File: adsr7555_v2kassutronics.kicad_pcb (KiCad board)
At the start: 2 copper layers, 68.6 x 104.1 mm, 47 parts, among them J1 Power, J2 GateIn, J5 Atn Out, J6 Output, Q1 3904, Q2 3904, Q3 3904, Q4 3904, SW1 SW_Push, U1 7555, U2 TL074

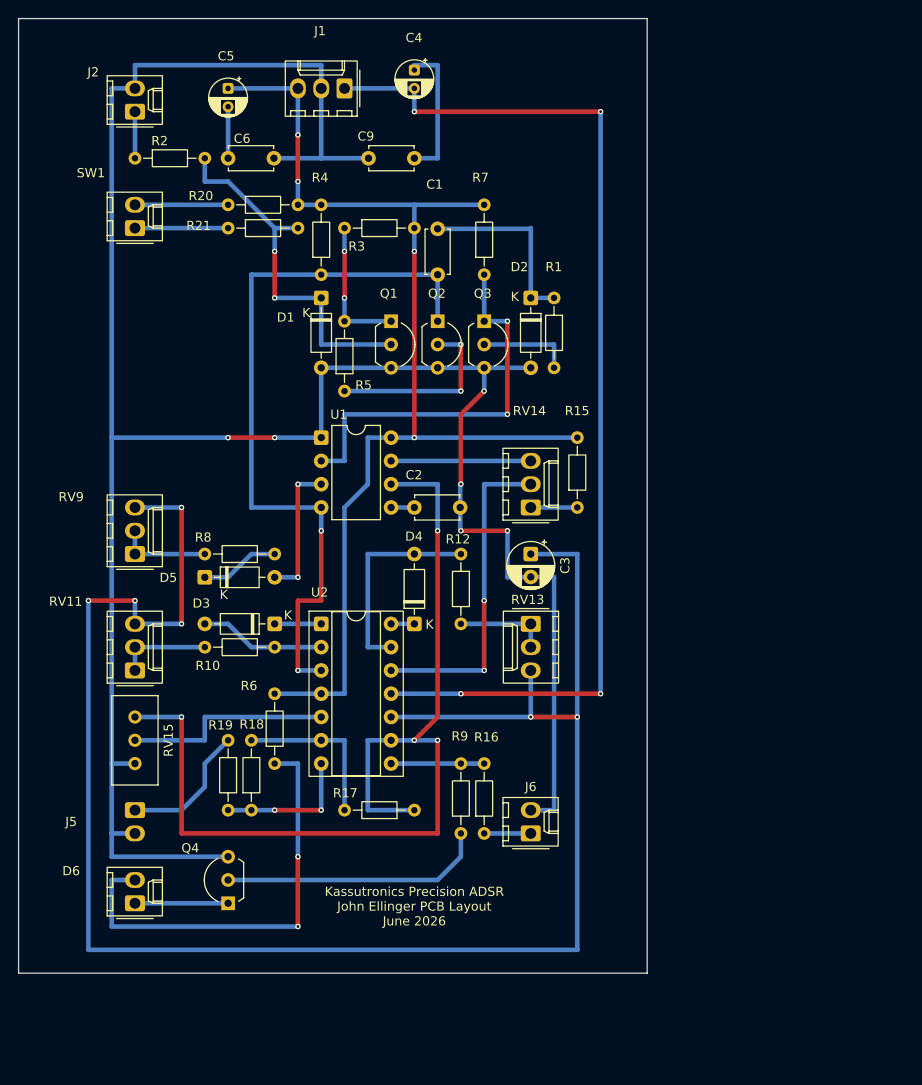
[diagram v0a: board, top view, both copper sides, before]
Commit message: archived v1 to jail. Redo for v2
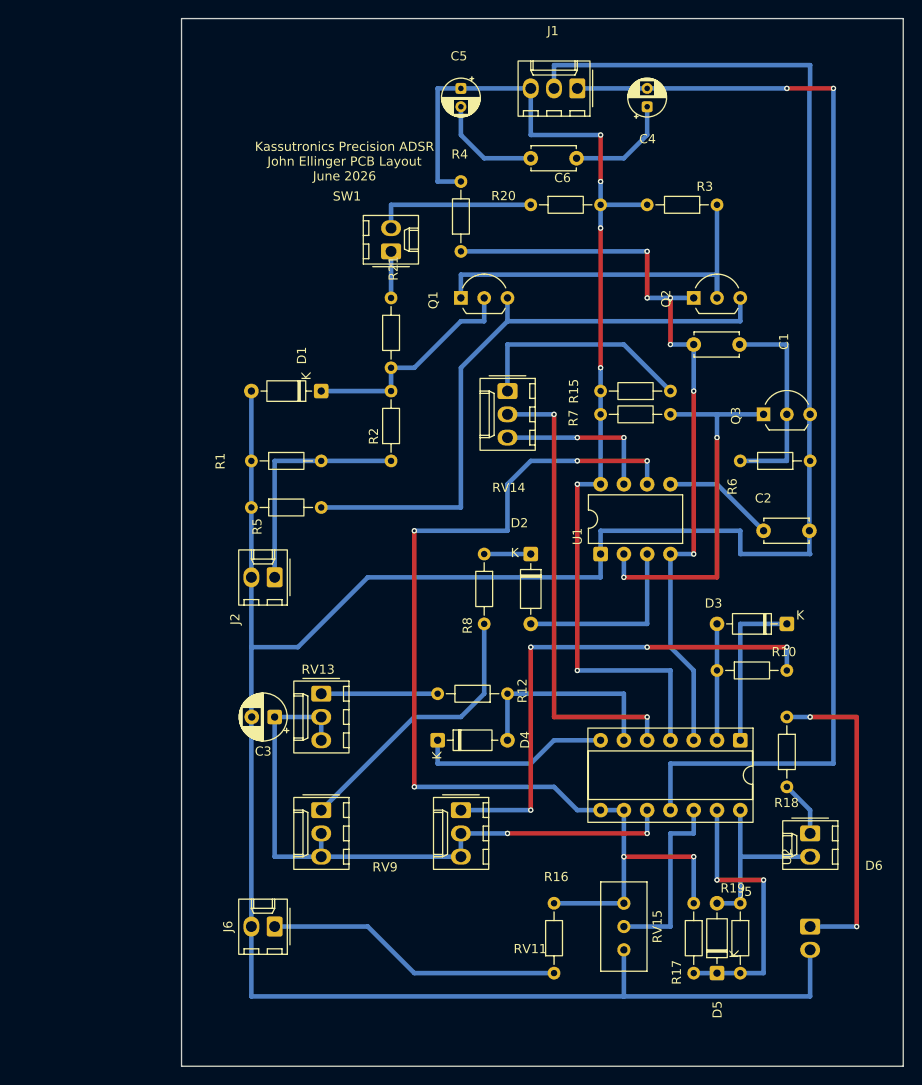
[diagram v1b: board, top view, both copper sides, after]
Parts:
- removed C9: 1n, Capacitor_THT:C_Disc_D4.7mm_W2.5mm_P5.00mm
- removed Q4: 3904, Package_TO_SOT_THT:TO-92L_Inline_Wide
- removed R9: 33k, Resistor_THT:R_Axial_DIN0204_L3.6mm_D1.6mm_P7.62mm_Horizontal
- R1: value 10k -> 1M-new
- R17: value 100k -> 4k7-x100k
- R18: value 100k -> 1k
- R19: value 1k -> 4k7
- R2: value 10k -> 1M-x10k
- R3: value 4k7 -> 47k-x4k7
- R4: value 4k7 -> 22k-x4k7
- R5: value 22k -> 10-new
- R6: value 4k7 -> 22k-new
- SW1: value SW_Push -> SW_Trig
- moved J5 74.7 mm to (109.2, 124.5)
- moved D6 74.1 mm to (109.2, 114.3), turned to -90 degrees
- moved D5 70.6 mm to (99.1, 129.5), turned to 90 degrees
- moved R6 67.1 mm to (109.2, 73.7), turned to 180 degrees
- moved R18 59.3 mm to (106.7, 101.6), turned to -90 degrees
- moved R19 58.6 mm to (101.6, 121.9)
- moved RV15 57.1 mm to (88.9, 127.0)
- moved D3 55.9 mm to (106.7, 91.4)
- moved J2 53.0 mm to (50.8, 86.4), turned to 180 degrees
- moved R10 48.3 mm to (99.1, 96.5), turned to 0 degrees
- moved U2 47.5 mm to (101.6, 104.1), turned to -90 degrees
- moved R2 43.3 mm to (63.5, 73.7), turned to 90 degrees
- moved R3 40.7 mm to (99.1, 45.7), turned to 180 degrees
- moved RV11 38.7 mm to (71.1, 111.8), turned to -90 degrees
- moved C2 38.2 mm to (104.1, 81.3)
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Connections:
- C1 pad 2: Net-(D2-K) -> Net-(Q3-B)
- C6 pad 1: Net-(C5-Pad2) -> Net-(C4-Pad1)
- C6 pad 2: GND -> Net-(C5-Pad2)
- D2 pad 2: GND -> Net-(D2-A)
- D6 pad 2: Net-(D6-A) -> Net-(D5-A)
- Q1 pad 3: GND -> Net-(Q1-E)
- Q2 pad 2: Net-(Q2-B) -> Net-(Q1-C)
- Q2 pad 3: GND -> Net-(Q1-E)
- R1 pad 1: Net-(D2-K) -> GND
- R1 pad 2: Net-(Q3-B) -> Net-(J2-Pin_1)
- R16 pad 2: Net-(R16-Pad2) -> Net-(U1-THRES)
- R17 pad 2: Net-(U2B--) -> Net-(D5-K)
- R18 pad 1: Net-(R18-Pad1) -> /ATTENOUT
- R18 pad 2: Net-(U2B--) -> Net-(D6-K)
- R19 pad 1: /ATTENOUT -> Net-(D5-A)
- R19 pad 2: Net-(R18-Pad1) -> Net-(D5-K)
- R5 pad 1: Net-(Q2-B) -> GND
- R5 pad 2: Net-(Q1-C) -> Net-(Q1-E)
- R6 pad 1: Net-(D6-A) -> GND
- R6 pad 2: +15V -> Net-(Q3-B)
- R8 pad 1: Net-(D5-K) -> Net-(D2-K)
- RV11 pad 2: Net-(R10-Pad2) -> Net-(U2C-+)
- RV13 pad 2: Net-(R12-Pad2) -> Net-(U2C-+)
- RV14 pad 2: Net-(U2D-+) -> Net-(U2B-+)
- RV15 pad 2: Net-(U2B-+) -> Net-(U2D-+)
- RV9 pad 2: Net-(R8-Pad2) -> Net-(U2C-+)
- U1 pad 3: Net-(D5-A) -> Net-(D2-A)
- U2 pad 13: Net-(D4-A) -> Net-(D5-K)
- U2 pad 14: Net-(D4-K) -> Net-(D5-A)
- U2 pad 6: Net-(U2B--) -> Net-(D4-A)
- U2 pad 7: Net-(R18-Pad1) -> Net-(D4-K)
- U2 pad 8: Net-(R16-Pad2) -> Net-(U1-THRES)
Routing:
- net Net-(U2C-+): track 195.6 -> 71.1 mm, vias 6 -> 2
- net Net-(Q1-E): track 0.00 -> 68.1 mm
- net Net-(D6-A): track 48.3 -> 0.00 mm, vias 2 -> 0
- net Net-(R10-Pad2): track 10.2 -> 55.9 mm, vias 0 -> 4
- net GND: track 262.9 -> 292.9 mm, vias 6 -> 0
- net Net-(Q4-B): track 29.0 -> 0.00 mm
- net Net-(Q1-C): track 15.2 -> 43.2 mm, vias 2 -> 0
- net Net-(U2B-+): track 22.9 -> 50.8 mm, vias 0 -> 2
- net /OUTPUT: track 5.08 -> 32.6 mm
- net Net-(D5-K): track 8.67 -> 30.5 mm, vias 0 -> 2
- net /ATTENOUT: track 14.8 -> 35.6 mm, vias 0 -> 2
- net Net-(R8-Pad2): track 10.2 -> 30.7 mm
- net Net-(Q2-B): track 20.3 -> 0.00 mm, vias 2 -> 0
- net Net-(J2-Pin_1): track 5.08 -> 25.4 mm
- net Net-(D2-A): track 0.00 -> 20.3 mm
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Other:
- board size 68.6 x 104.1 mm -> 78.7 x 114.3 mm
- board text added: "Main Sheet"

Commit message: added pdfs for sch and pcb
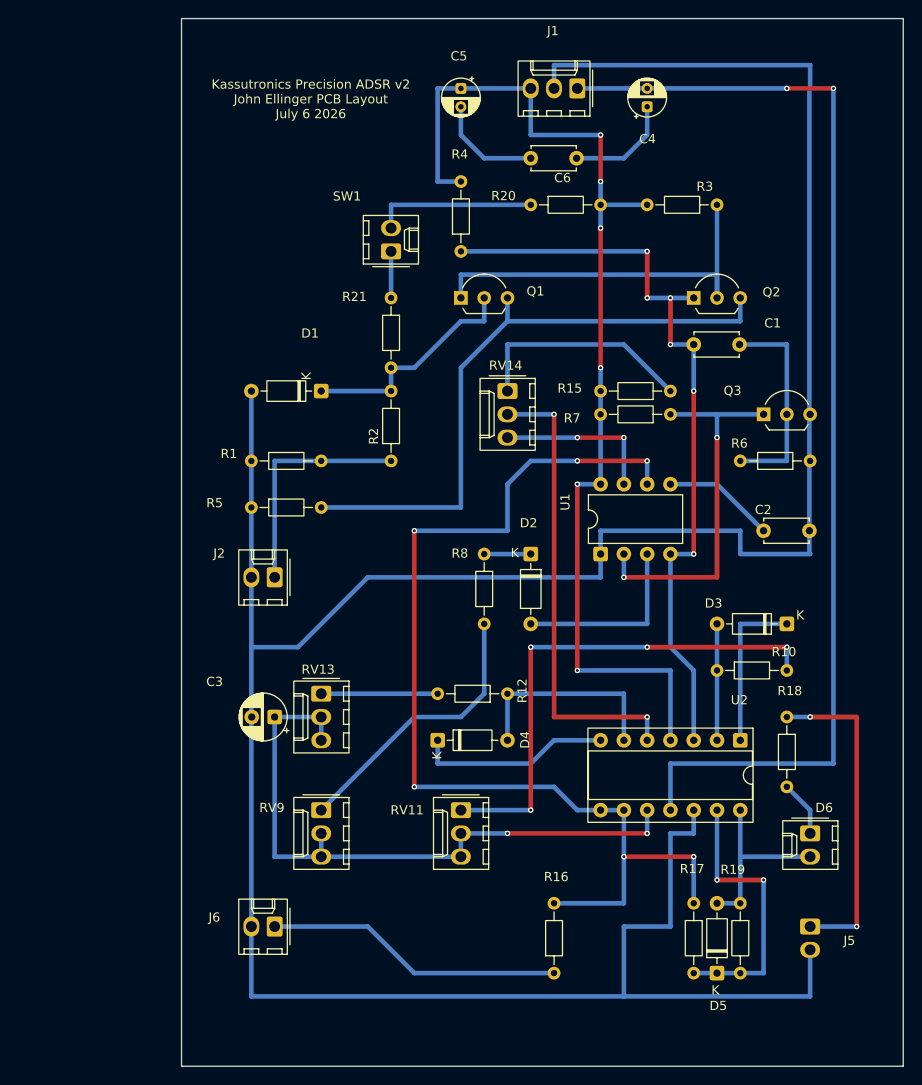
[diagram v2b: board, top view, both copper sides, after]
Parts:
- removed RV15: 100k Lin Atn, Potentiometer_THT:Potentiometer_Bourns_3296W_Vertical
- R7: value 4k7 -> 22k-x4k7
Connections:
- net /ATTENOUT renamed /INVOUT
- net Net-(U1-THRES) renamed /THR
- U2 pad 12: Net-(U2D-+) -> GND
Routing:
- net GND: track 292.9 -> 315.8 mm
- net Net-(U2D-+): track 20.3 -> 0.00 mm
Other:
- board text added: "Kassutronics Precision ADSR v2 John Ellinger PCB Layout July 6 2026"
- board text removed: "Kassutronics Precision ADSR John Ellinger PCB Layout June 2026"

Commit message: modified wiring on U2D
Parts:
- J5: value Atn Out -> InvOut
- R1: value 1M-new -> 1M
- R17: value 4k7-x100k -> 4k7
- R2: value 1M-x10k -> 1M
- R3: value 47k-x4k7 -> 47k
- R4, R7: value 22k-x4k7 -> 22k
- R5: value 10-new -> 10
- R6: value 22k-new -> 22k
- moved R19 5.68 mm to (104.1, 116.8)
- moved D5 5.68 mm to (101.6, 124.5)
- moved R17 3.59 mm to (99.1, 124.5), turned to 90 degrees
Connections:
- net /GATE renamed GATE
- net /INVOUT renamed Net-(J5-Pin_1)
- net /OUTPUT renamed Net-(J6-Pin_1)
- net /THR renamed THR
- net /TRIG renamed TRIG
- C4 pad 1: Net-(C4-Pad1) -> Net-(J1-Pin_1)
- C5 pad 2: Net-(C5-Pad2) -> Net-(J1-Pin_3)
- C6 pad 1: Net-(C4-Pad1) -> -15V
- C6 pad 2: Net-(C5-Pad2) -> +15V
- D6 pad 1: Net-(D6-K) -> Net-(D5-A)
- D6 pad 2: Net-(D5-A) -> Net-(D6-A)
- J1 pad 1: -15V -> Net-(J1-Pin_1)
- J1 pad 3: +15V -> Net-(J1-Pin_3)
- R18 pad 2: Net-(D6-K) -> Net-(D6-A)
- R19 pad 1: Net-(D5-A) -> Net-(D6-A)
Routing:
- net Net-(D6-A): track 0.00 -> 15.2 mm, vias 0 -> 2
- net Net-(D5-K): track 30.5 -> 16.3 mm, vias 2 -> 0
- net Net-(C4-Pad1): track 11.8 -> 0.00 mm
- net Net-(C5-Pad2): track 11.8 -> 0.00 mm
- net -15V: track 124.5 -> 134.7 mm
- net +15V: track 119.4 -> 109.8 mm, vias 6 -> 4
- net Net-(J1-Pin_1): track 0.00 -> 8.45 mm
- net Net-(J1-Pin_3): track 0.00 -> 8.45 mm
- net Net-(D5-A): track 20.3 -> 13.8 mm
- net Net-(D6-K): track 6.13 -> 0.00 mm
- net THR: track 116.4 -> 121.5 mm
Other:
- board text added: "Kassutronics Precision ADSR v2 John Ellinger PCB Layout Oct 22 2026 537x780 px"
- board text removed: "Kassutronics Precision ADSR v2 John Ellinger PCB Layout July 6 2026"

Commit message: checking PCB wiring
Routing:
- net Net-(J5-Pin_1): track 35.6 -> 28.5 mm

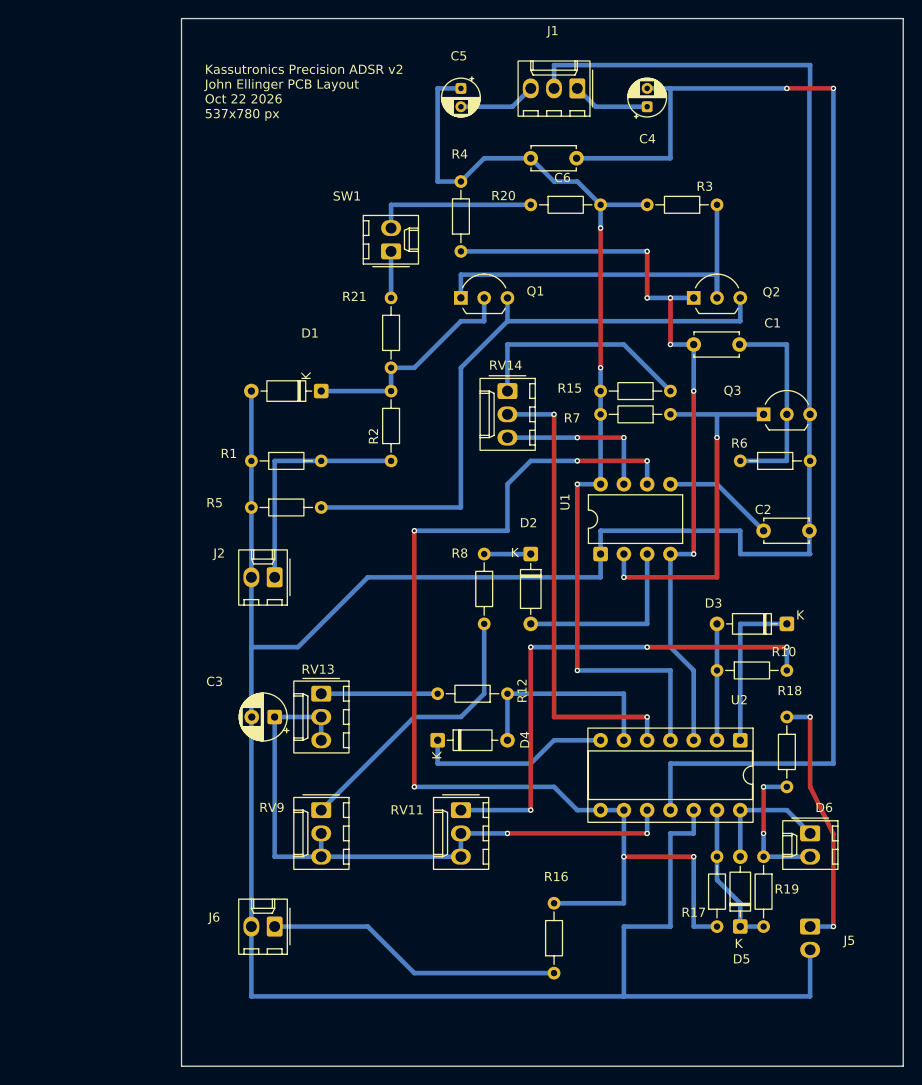
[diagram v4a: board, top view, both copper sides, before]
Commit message: cleaned up PCB wiring and designators
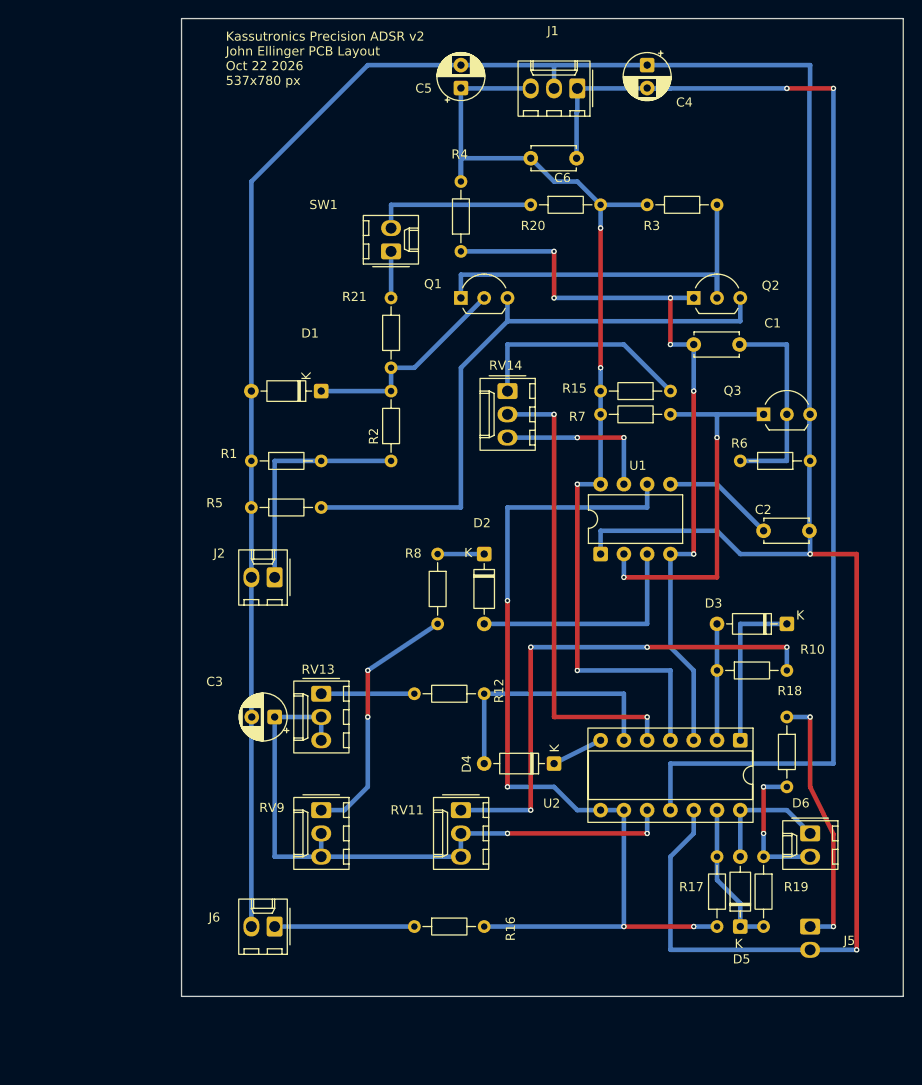
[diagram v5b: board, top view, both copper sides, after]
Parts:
- C4, C5: footprint Capacitor_THT:CP_Radial_D4.0mm_P2.00mm -> Capacitor_THT:CP_Radial_D5.0mm_P2.50mm
- moved R16 16.1 mm to (66.0, 124.5), turned to 0 degrees
- moved D4 13.0 mm to (81.3, 106.7), turned to 180 degrees
- moved D2 5.08 mm to (73.7, 83.8)
- moved R8 5.08 mm to (68.6, 83.8)
- moved C4 4.54 mm to (91.4, 30.5), turned to -90 degrees
- moved R12 2.54 mm to (73.7, 99.1)
- turned C5 to 90 degrees
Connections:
- C4 pad 1: Net-(J1-Pin_1) -> GND
- C5 pad 2: Net-(J1-Pin_3) -> GND
- J1 pad 1: Net-(J1-Pin_1) -> -15V
- J1 pad 3: Net-(J1-Pin_3) -> +15V
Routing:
- net THR: track 121.5 -> 100.1 mm, vias 6 -> 4
- net Net-(J6-Pin_1): track 32.6 -> 15.2 mm
- net Net-(D4-K): track 21.4 -> 5.68 mm
- net Net-(J1-Pin_1): track 8.45 -> 0.00 mm
- net Net-(J1-Pin_3): track 8.45 -> 0.00 mm
- net Net-(D4-A): track 22.9 -> 27.9 mm
- net Net-(D2-A): track 20.3 -> 25.4 mm
- net +15V: track 109.8 -> 113.9 mm
- net Net-(R8-Pad2): track 30.7 -> 28.0 mm, vias 0 -> 2
- net Net-(R12-Pad2): track 12.7 -> 10.2 mm
- net Net-(D1-K): track 25.0 -> 23.5 mm
- net GND: track 315.6 -> 314.7 mm, vias 0 -> 2
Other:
- board size 78.7 x 114.3 mm -> 78.7 x 106.7 mm

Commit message: added PCB screenshot png
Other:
- board text added: "Kassutronics Precision ADSR v2 John Ellinger PCB Layout Oct 22 2026 580x782 px"
- board text removed: "Kassutronics Precision ADSR v2 John Ellinger PCB Layout Oct 22 2026 537x780 px"
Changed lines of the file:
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@@
 	(title_block
 		(title "Kassutronics Precision ADSR v2")
-		(date "2026-07-06")
-		(rev "01")
+		(date "2026-10-25")
+		(rev "02")
 		(company "John Ellinger")
 	)
@@
 		(layer "User.15")
 	)
-	(gr_text "Kassutronics Precision ADSR v2\nJohn Ellinger PCB Layout\nOct 22 2026\n537x780 px"
+	(gr_text "Kassutronics Precision ADSR v2\nJohn Ellinger PCB Layout\nOct 22 2026\n580x782 px"
 		(at 45.466 32.766 0)
 		(layer "F.SilkS")

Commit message: added .svg wiring +15 -15, GND in progress
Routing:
- net GND: track 314.7 -> 331.8 mm
- net +15V: track 113.9 -> 109.9 mm
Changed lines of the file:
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@@
 		(tags "Resistor Axial_DIN0204 series Axial Horizontal pin pitch 7.62mm 0.167W length 3.6mm diameter 1.6mm")
 		(property "Reference" "R4"
-			(at 10.59 -0.13 0)
+			(at 10.16 -2.54 0)
 			(layer "F.SilkS")
 			(effects
@@
 		)
 		(property "Value" "22k"
-			(at 9.34 -0.13 0)
+			(at 8.91 -2.54 0)
 			(layer "F.Fab")
 			(effects
@@
 		)
 		(property "Value" "InvOut"
-			(at 5.54 -3.53 180)
+			(at 5.54 -3.53 0)
 			(layer "F.Fab")
 			(effects
@@
 	)
 	(segment
+		(start 48.26 78.74)
+		(end 45.72 78.74)
+		(width 0.5)
+		(layer "B.Cu")
+		(net "GND")
+	)
+	(segment
 		(start 109.22 83.82)
 		(end 101.6 83.82)
@@
 	)
 	(segment
+		(start 45.72 66.04)
+		(end 45.72 43.18)
+		(width 0.5)
+		(layer "B.Cu")
+		(net "GND")
+	)
+	(segment
 		(start 109.22 33.02)
 		(end 109.14 33.1)
@@
 	)
 	(segment
-		(start 48.26 66.04)
-		(end 48.26 124.46)
+		(start 60.96 30.48)
+		(end 71.12 30.48)
 		(width 0.5)
 		(layer "B.Cu")
@@
 	)
 	(segment
+		(start 48.26 73.66)
+		(end 45.72 73.66)
+		(width 0.5)
+		(layer "B.Cu")
+		(net "GND")
+	)
+	(segment
 		(start 96.52 111.76)
 		(end 96.52 114.3)
@@
 	)
 	(segment
+		(start 45.72 78.74)
+		(end 45.72 73.66)
+		(width 0.5)
+		(layer "B.Cu")
+		(net "GND")
+	)
+	(segment
 		(start 93.98 116.84)
 		(end 93.98 127)
@@
 	)
 	(segment
-		(start 60.96 30.48)
-		(end 71.12 30.48)
+		(start 48.26 86.36)
+		(end 45.72 86.36)
 		(width 0.5)
 		(layer "B.Cu")
@@
 	)
 	(segment
+		(start 48.3 101.6)
+		(end 45.72 101.6)
+		(width 0.5)
+		(layer "B.Cu")
+		(net "GND")
+	)
+	(segment
+		(start 45.72 101.6)
+		(end 45.72 86.36)
+		(width 0.5)
+		(layer "B.Cu")
+		(net "GND")
+	)
+	(segment
+		(start 45.72 73.66)
+		(end 45.72 66.04)
+		(width 0.5)
+		(layer "B.Cu")
+		(net "GND")
+	)
+	(segment
+		(start 45.72 124.46)
+		(end 45.72 101.6)
+		(width 0.5)
+		(layer "B.Cu")
+		(net "GND")
+	)
+	(segment
 		(start 71.12 30.48)
 		(end 81.28 30.48)
@@
 	(segment
 		(start 48.26 66.04)
-		(end 48.26 43.18)
-		(width 0.5)
-		(layer "B.Cu")
-		(net "GND")
-	)
-	(segment
-		(start 48.26 43.18)
-		(end 60.96 30.48)
+		(end 45.72 66.04)
+		(width 0.5)
+		(layer "B.Cu")
+		(net "GND")
+	)
+	(segment
+		(start 48.26 124.46)
+		(end 45.72 124.46)
 		(width 0.5)
 		(layer "B.Cu")
@@
 	)
 	(segment
+		(start 45.72 43.18)
+		(end 60.96 30.48)
+		(width 0.5)
+		(layer "B.Cu")
+		(net "GND")
+	)
+	(segment
 		(start 114.3 127)
 		(end 109.22 127)
@@
 	)
 	(segment
+		(start 45.72 86.36)
+		(end 45.72 78.74)
+		(width 0.5)
+		(layer "B.Cu")
+		(net "GND")
+	)
+	(segment
 		(start 109.22 127)
 		(end 93.98 127)
@@
 	)
 	(segment
+		(start 91.44 96.52)
+		(end 93.98 99.06)
+		(width 0.5)
+		(layer "F.Cu")
+		(net "+15V")
+	)
+	(segment
+		(start 93.98 99.06)
+		(end 93.98 101.6)
+		(width 0.5)
+		(layer "F.Cu")
+		(net "+15V")
+	)
+	(segment
+		(start 86.36 63.5)
+		(end 86.36 48.26)
+		(width 0.5)
+		(layer "F.Cu")
+		(net "+15V")
+	)
+	(segment
+		(start 83.82 96.52)
+		(end 91.44 96.52)
+		(width 0.5)
+		(layer "F.Cu")
+		(net "+15V")
+	)
+	(segment
 		(start 83.82 76.2)
 		(end 83.82 96.52)
@@
 		(net "+15V")
 	)
-	(segment
-		(start 86.36 63.5)
-		(end 86.36 48.26)
-		(width 0.5)
-		(layer "F.Cu")
-		(net "+15V")
-	)
 	(via
 		(at 83.82 76.2)
@@
 	)
 	(via
+		(at 93.98 101.6)
+		(size 0.6)
+		(drill 0.3)
+		(layers "F.Cu" "B.Cu")
+		(net "+15V")
+	)
+	(via
 		(at 86.36 63.5)
 		(size 0.6)
@@
 	(via
 		(at 86.36 48.26)
-		(size 0.6)
-		(drill 0.3)
-		(layers "F.Cu" "B.Cu")
-		(net "+15V")
-	)
-	(via
-		(at 83.82 96.52)
 		(size 0.6)
 		(drill 0.3)
@@
 	)
 	(segment
-		(start 71.12 40.64)
+		(start 71.12 32.98)
 		(end 71.12 43.18)
 		(width 0.5)
@@
 	)
 	(segment
-		(start 78.74 40.64)
-		(end 71.12 40.64)
+		(start 93.98 104.14)
+		(end 93.98 101.6)
 		(width 0.5)
 		(layer "B.Cu")
@@
 	)
 	(segment
-		(start 93.98 104.14)
-		(end 93.98 96.52)
-		(width 0.5)
-		(layer "B.Cu")
-		(net "+15V")
-	)
-	(segment
 		(start 78.74 40.64)
 		(end 81.28 43.18)
@@
 	)
 	(segment
-		(start 71.12 33.02)
-		(end 71.12 43.18)
+		(start 78.74 33.02)
+		(end 78.74 40.64)
 		(width 0.5)
 		(layer "B.Cu")
@@
 		(width 0.5)
 		(layer "B.Cu")
-		(net "+15V")
-	)
-	(segment
-		(start 93.98 96.52)
-		(end 83.82 96.52)
-		(width 0.5)
-		(layer "B.Cu")
